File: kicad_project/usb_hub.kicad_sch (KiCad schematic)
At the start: 52 parts, among them J1 USB4105-GF-A, J2 UJ2-ADH-3-TH, U2 CY7C65632-48AXCT, U3 USBLC6-2SC6, U4 USBLC6-2SC6, U5 USBLC6-2SC6, U6 BD2221G-LBTR, U7 BD2221G-LBTR

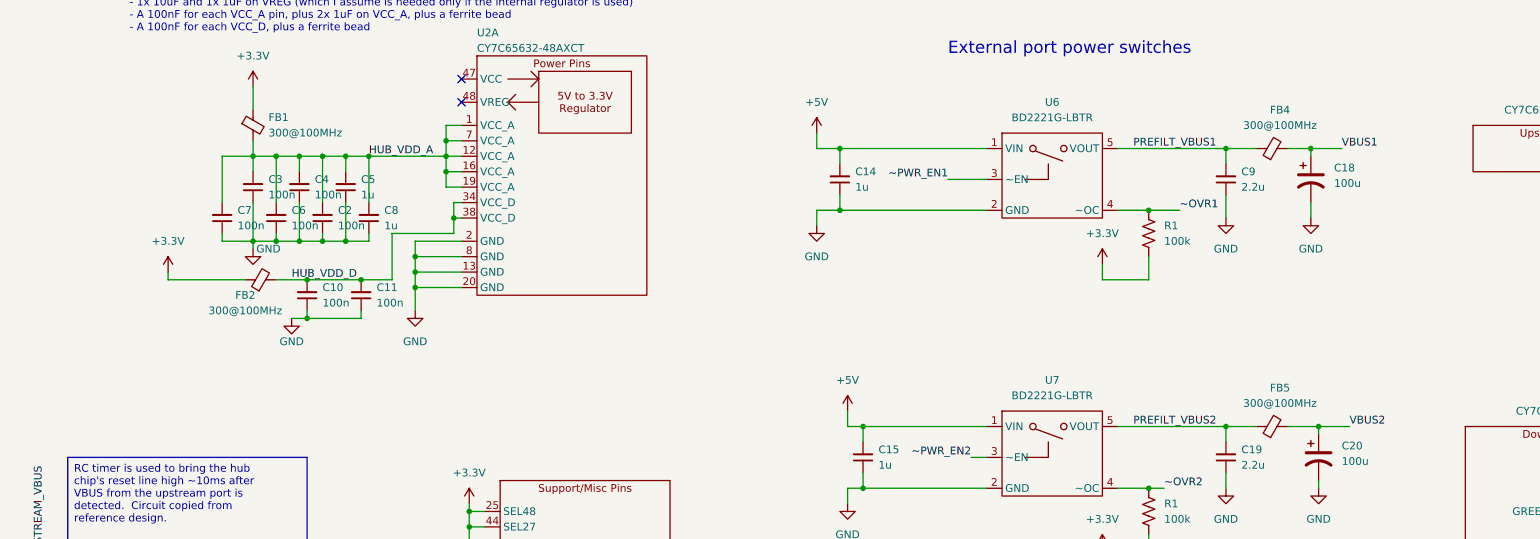
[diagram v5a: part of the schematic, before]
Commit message: Add logo to PCB, add last labels, fix DRC
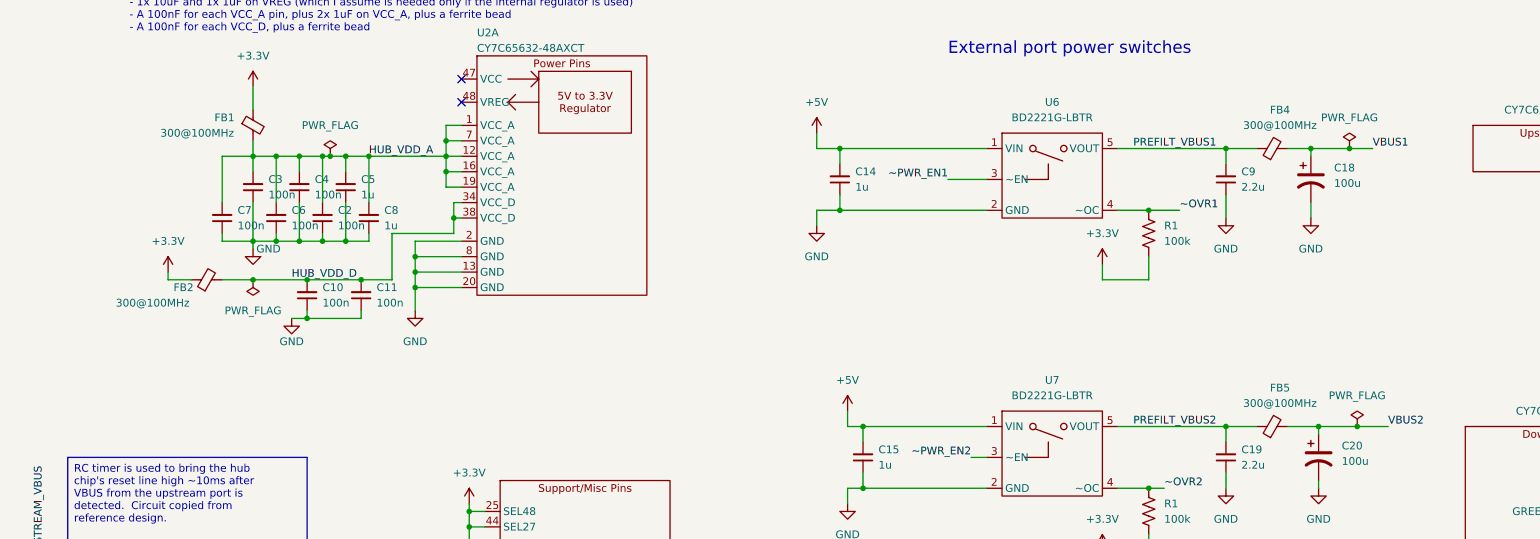
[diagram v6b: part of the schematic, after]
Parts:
- J1: footprint Connector_USB:USB_C_Receptacle_GCT_USB4105-xx-A_16P_TopMnt_Horizontal -> project libraries:USB_C_Receptacle_GCT_USB4105-xx-A_16P_TopMnt_Horizontal-ExtraHoleClearance
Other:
- moved on the sheet: FB2
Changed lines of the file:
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@@
   (junction (at 62.23 48.26) (diameter 0) (color 0 0 0 0)
   )
+  (junction (at 240.03 92.71) (diameter 0) (color 0 0 0 0)
+  )
   (junction (at 68.58 240.03) (diameter 0) (color 0 0 0 0)
   )
@@
   (junction (at 66.04 48.26) (diameter 0) (color 0 0 0 0)
   )
+  (junction (at 238.76 46.99) (diameter 0) (color 0 0 0 0)
+  )
   (junction (at 62.23 62.23) (diameter 0) (color 0 0 0 0)
   )
@@
   (junction (at 335.28 229.87) (diameter 0) (color 0 0 0 0)
   )
+  (junction (at 71.12 48.26) (diameter 0) (color 0 0 0 0)
+  )
   (junction (at 85.09 67.31) (diameter 0) (color 0 0 0 0)
   )
@@
   (junction (at 93.98 109.22) (diameter 0) (color 0 0 0 0)
   )
+  (junction (at 58.42 68.58) (diameter 0) (color 0 0 0 0)
+  )
   (junction (at 347.98 120.65) (diameter 0) (color 0 0 0 0)
   )
@@
     (stroke (width 0) (type default))
   )
-  (wire (pts (xy 62.23 68.58) (xy 67.31 68.58))
+  (wire (pts (xy 53.34 68.58) (xy 58.42 68.58))
     (stroke (width 0) (type default))
   )
@@
     (stroke (width 0) (type default))
   )
-  (wire (pts (xy 44.45 68.58) (xy 57.15 68.58))
+  (wire (pts (xy 44.45 68.58) (xy 48.26 68.58))
     (stroke (width 0) (type default))
   )
@@
     (stroke (width 0) (type default))
   )
-  (wire (pts (xy 233.68 92.71) (xy 238.76 92.71))
+  (wire (pts (xy 233.68 92.71) (xy 240.03 92.71))
     (stroke (width 0) (type default))
   )
@@
     (stroke (width 0) (type default))
   )
-  (wire (pts (xy 232.41 46.99) (xy 237.49 46.99))
-    (stroke (width 0) (type default))
-  )
   (wire (pts (xy 318.77 214.63) (xy 318.77 219.71))
     (stroke (width 0) (type default))
@@
     (stroke (width 0) (type default))
   )
+  (wire (pts (xy 238.76 46.99) (xy 242.57 46.99))
+    (stroke (width 0) (type default))
+  )
   (wire (pts (xy 182.88 205.74) (xy 199.39 205.74))
     (stroke (width 0) (type default))
@@
     (stroke (width 0) (type default))
   )
+  (wire (pts (xy 71.12 48.26) (xy 69.85 48.26))
+    (stroke (width 0) (type default))
+  )
   (wire (pts (xy 335.28 229.87) (xy 351.79 229.87))
     (stroke (width 0) (type default))
@@
     (stroke (width 0) (type default))
   )
-  (wire (pts (xy 73.66 48.26) (xy 69.85 48.26))
+  (wire (pts (xy 73.66 48.26) (xy 71.12 48.26))
     (stroke (width 0) (type default))
   )
@@
     (stroke (width 0) (type default))
   )
+  (wire (pts (xy 232.41 46.99) (xy 238.76 46.99))
+    (stroke (width 0) (type default))
+  )
   (wire (pts (xy 344.17 133.35) (xy 360.68 133.35))
     (stroke (width 0) (type default))
@@
     (stroke (width 0) (type default))
   )
+  (wire (pts (xy 58.42 68.58) (xy 67.31 68.58))
+    (stroke (width 0) (type default))
+  )
   (wire (pts (xy 241.3 213.36) (xy 241.3 215.9))
     (stroke (width 0) (type default))
@@
     (stroke (width 0) (type default))
   )
+  (wire (pts (xy 240.03 92.71) (xy 245.11 92.71))
+    (stroke (width 0) (type default))
+  )
   (wire (pts (xy 204.47 218.44) (xy 204.47 228.6))
     (stroke (width 0) (type default))
@@
     (effects (font (size 1.27 1.27)) (justify left bottom))
   )
-  (label "VBUS2" (at 238.76 92.71 0) (fields_autoplaced)
+  (label "VBUS2" (at 245.11 92.71 0) (fields_autoplaced)
     (effects (font (size 1.27 1.27)) (justify left bottom))
   )
@@
     (effects (font (size 1.27 1.27)) (justify left bottom))
   )
-  (label "VBUS1" (at 237.49 46.99 0) (fields_autoplaced)
+  (label "VBUS1" (at 242.57 46.99 0) (fields_autoplaced)
     (effects (font (size 1.27 1.27)) (justify left bottom))
   )
@@
     )
   )
+  (symbol (lib_id "power:PWR_FLAG") (at 58.42 68.58 180) (unit 1)
+    (in_bom yes) (on_board yes) (dnp no) (fields_autoplaced)
+    (property "Reference" "#FLG05" (at 58.42 70.485 0)
+      (effects (font (size 1.27 1.27)) hide)
+    )
+    (property "Value" "PWR_FLAG" (at 58.42 73.66 0)
+      (effects (font (size 1.27 1.27)))
+    )
+    (property "Footprint" "" (at 58.42 68.58 0)
+      (effects (font (size 1.27 1.27)) hide)
+    )
+    (property "Datasheet" "~" (at 58.42 68.58 0)
+      (effects (font (size 1.27 1.27)) hide)
+    )
+    (pin "1")
+    (instances
+      (project "mbed-ce-ci-shield-v2"
+        (path "/a0f40274-9469-4bcf-885c-e8b8a490ea54/d2cb7c4f-a03f-4f1c-8cab-0427a0ad2909"
+          (reference "#FLG05") (unit 1)
+        )
+      )
+    )
+  )
   (symbol (lib_id "power:+5V") (at 156.21 90.17 0) (unit 1)
     (in_bom yes) (on_board yes) (dnp no) (fields_autoplaced)
@@
     )
   )
+  (symbol (lib_id "power:PWR_FLAG") (at 238.76 46.99 0) (unit 1)
+    (in_bom yes) (on_board yes) (dnp no) (fields_autoplaced)
+    (property "Reference" "#FLG06" (at 238.76 45.085 0)
+      (effects (font (size 1.27 1.27)) hide)
+    )
+    (property "Value" "PWR_FLAG" (at 238.76 41.91 0)
+      (effects (font (size 1.27 1.27)))
+    )
+    (property "Footprint" "" (at 238.76 46.99 0)
+      (effects (font (size 1.27 1.27)) hide)
+    )
+    (property "Datasheet" "~" (at 238.76 46.99 0)
+      (effects (font (size 1.27 1.27)) hide)
+    )
+    (pin "1")
+    (instances
+      (project "mbed-ce-ci-shield-v2"
+        (path "/a0f40274-9469-4bcf-885c-e8b8a490ea54/d2cb7c4f-a03f-4f1c-8cab-0427a0ad2909"
+          (reference "#FLG06") (unit 1)
+        )
+      )
+    )
+  )
   (symbol (lib_id "Device:C_Polarized_US") (at 232.41 52.07 0) (unit 1)
     (in_bom yes) (on_board yes) (dnp no) (fields_autoplaced)
@@
       (effects (font (size 1.27 1.27)) (justify right))
     )
-    (property "Footprint" "Connector_USB:USB_C_Receptacle_GCT_USB4105-xx-A_16P_TopMnt_Horizontal" (at 372.11 57.15 0)
+    (property "Footprint" "project libraries:USB_C_Receptacle_GCT_USB4105-xx-A_16P_TopMnt_Horizontal-ExtraHoleClearance" (at 372.11 57.15 0)
       (effects (font (size 1.27 1.27)) hide)
     )
@@
   )
   (symbol (lib_id "Device:FerriteBead_Small") (at 58.42 43.18 0) (unit 1)
-    (in_bom yes) (on_board yes) (dnp no) (fields_autoplaced)
-    (property "Reference" "FB1" (at 60.96 41.8719 0)
+    (in_bom yes) (on_board yes) (dnp no)
+    (property "Reference" "FB1" (at 52.07 41.91 0)
       (effects (font (size 1.27 1.27)) (justify left))
     )
-    (property "Value" "300@100MHz" (at 60.96 44.4119 0)
+    (property "Value" "300@100MHz" (at 43.18 44.45 0)
       (effects (font (size 1.27 1.27)) (justify left))
     )
@@
     )
   )
+  (symbol (lib_id "power:PWR_FLAG") (at 240.03 92.71 0) (unit 1)
+    (in_bom yes) (on_board yes) (dnp no) (fields_autoplaced)
+    (property "Reference" "#FLG07" (at 240.03 90.805 0)
+      (effects (font (size 1.27 1.27)) hide)
+    )
+    (property "Value" "PWR_FLAG" (at 240.03 87.63 0)
+      (effects (font (size 1.27 1.27)))
+    )
+    (property "Footprint" "" (at 240.03 92.71 0)
+      (effects (font (size 1.27 1.27)) hide)
+    )
+    (property "Datasheet" "~" (at 240.03 92.71 0)
+      (effects (font (size 1.27 1.27)) hide)
+    )
+    (pin "1")
+    (instances
+      (project "mbed-ce-ci-shield-v2"
+        (path "/a0f40274-9469-4bcf-885c-e8b8a490ea54/d2cb7c4f-a03f-4f1c-8cab-0427a0ad2909"
+          (reference "#FLG07") (unit 1)
+        )
+      )
+    )
+  )
   (symbol (lib_id "power:GND") (at 68.58 243.84 0) (unit 1)
     (in_bom yes) (on_board yes) (dnp no)
@@
     )
   )
+  (symbol (lib_id "power:PWR_FLAG") (at 71.12 48.26 0) (unit 1)
+    (in_bom yes) (on_board yes) (dnp no) (fields_autoplaced)
+    (property "Reference" "#FLG04" (at 71.12 46.355 0)
+      (effects (font (size 1.27 1.27)) hide)
+    )
+    (property "Value" "PWR_FLAG" (at 71.12 43.18 0)
+      (effects (font (size 1.27 1.27)))
+    )
+    (property "Footprint" "" (at 71.12 48.26 0)
+      (effects (font (size 1.27 1.27)) hide)
+    )
+    (property "Datasheet" "~" (at 71.12 48.26 0)
+      (effects (font (size 1.27 1.27)) hide)
+    )
+    (pin "1")
+    (instances
+      (project "mbed-ce-ci-shield-v2"
+        (path "/a0f40274-9469-4bcf-885c-e8b8a490ea54/d2cb7c4f-a03f-4f1c-8cab-0427a0ad2909"
+          (reference "#FLG04") (unit 1)
+        )
+      )
+    )
+  )
   (symbol (lib_id "Device:C_Small") (at 154.94 52.07 180) (unit 1)
     (in_bom yes) (on_board yes) (dnp no) (fields_autoplaced)
@@
     )
   )
-  (symbol (lib_id "Device:FerriteBead_Small") (at 59.69 68.58 90) (unit 1)
+  (symbol (lib_id "Device:FerriteBead_Small") (at 50.8 68.58 90) (unit 1)
     (in_bom yes) (on_board yes) (dnp no)
-    (property "Reference" "FB2" (at 57.15 71.12 90)
+    (property "Reference" "FB2" (at 46.99 69.85 90)
       (effects (font (size 1.27 1.27)))
     )
-    (property "Value" "300@100MHz" (at 57.15 73.66 90)
+    (property "Value" "300@100MHz" (at 41.91 72.39 90)
       (effects (font (size 1.27 1.27)))
     )
-    (property "Footprint" "Resistor_SMD:R_1206_3216Metric" (at 59.69 70.358 90)
+    (property "Footprint" "Resistor_SMD:R_1206_3216Metric" (at 50.8 70.358 90)
       (effects (font (size 1.27 1.27)) hide)
     )
-    (property "Datasheet" "~" (at 59.69 68.58 0)
+    (property "Datasheet" "~" (at 50.8 68.58 0)
       (effects (font (size 1.27 1.27)) hide)
     )
-    (property "SKU" "732-4654-1-ND" (at 59.69 68.58 0)
+    (property "SKU" "732-4654-1-ND" (at 50.8 68.58 0)
       (effects (font (size 1.27 1.27)) hide)
     )

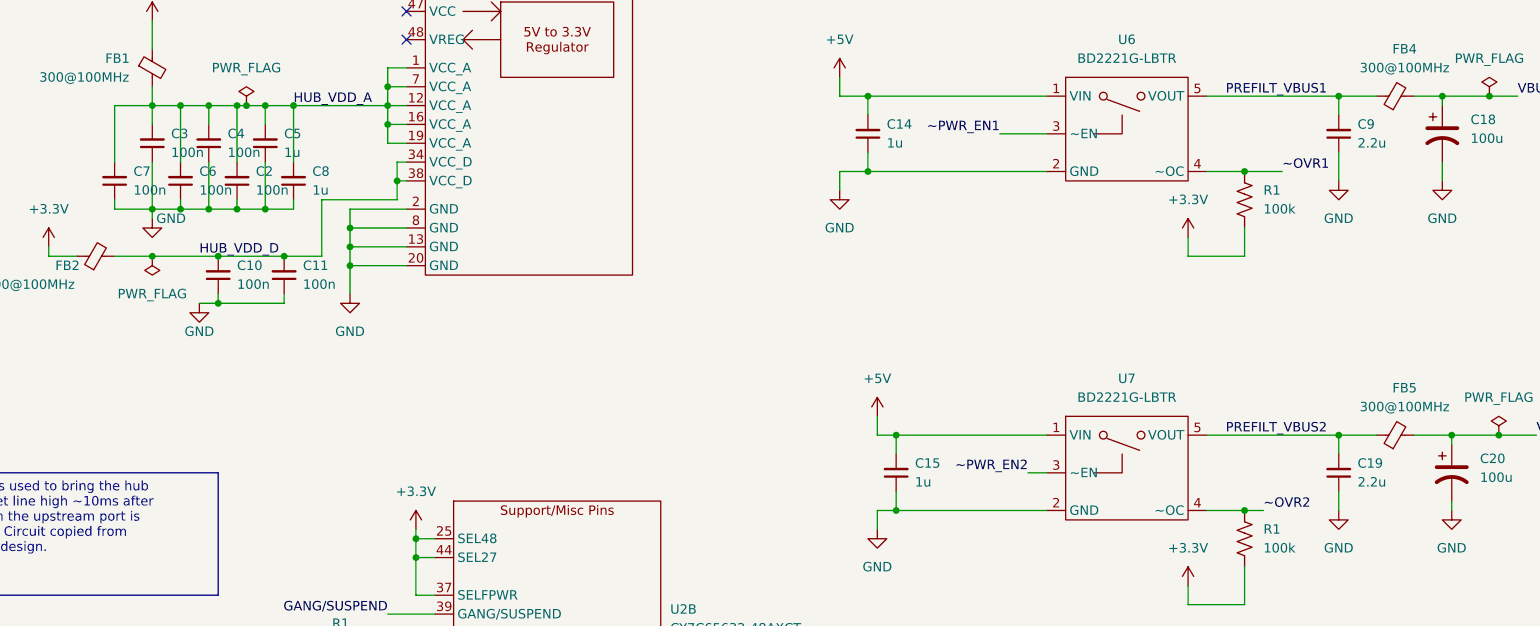
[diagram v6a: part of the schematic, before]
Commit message: Add part numbers for capacitors, start working on BoM job
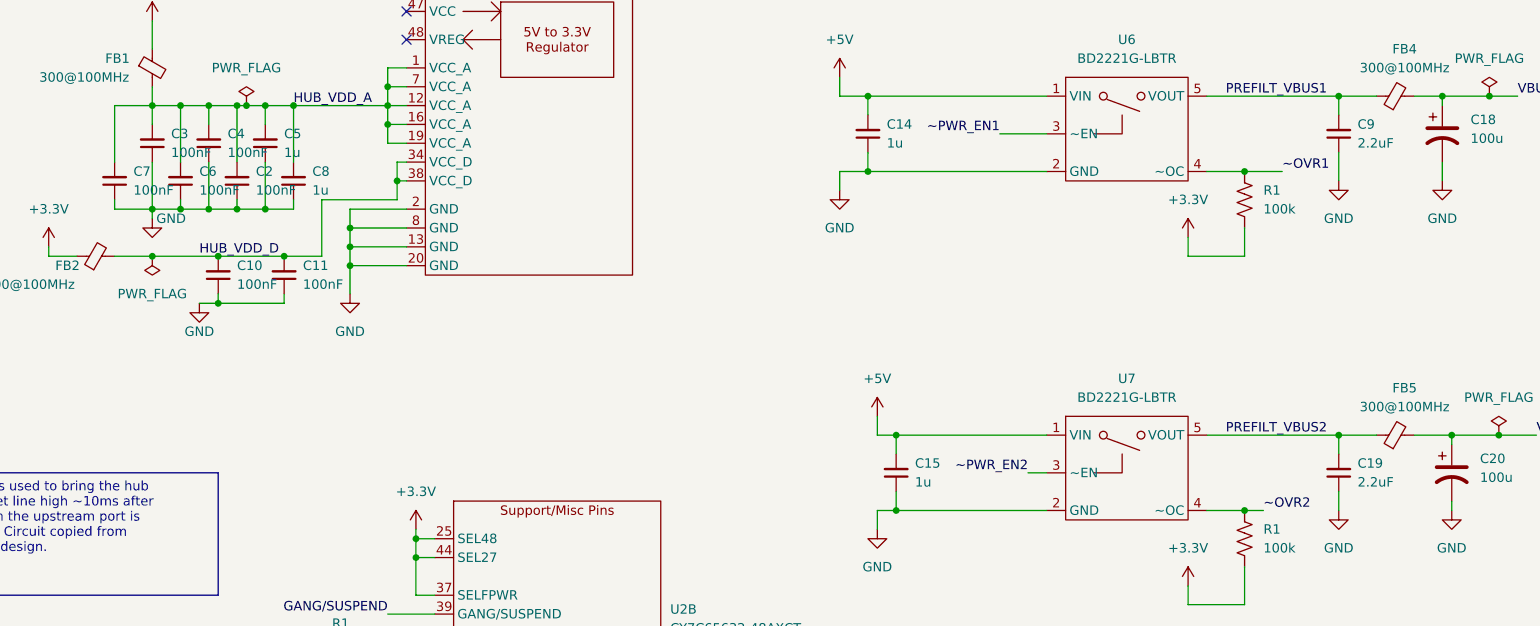
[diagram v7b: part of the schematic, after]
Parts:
- C10, C11, C2, C3, C4, C6, C7: value 100n -> 100nF; LibRef (none) -> GRM319R72A104KA01D; Supplier (none) -> Digi-Key
- C14, C15, C21, C5, C8: LibRef (none) -> CL31B105KBHNNNE; Supplier (none) -> Digi-Key
- C18: LibRef (none) -> RL81V101MDN1KX; Supplier (none) -> Digi-Key
- C19, C9: value 2.2u -> 2.2uF; LibRef (none) -> CL31B225KBHNNNE; SKU (none) -> 1276-1291-1-ND; Supplier (none) -> Digi-Key
- C20: LibRef (none) -> RL81V101MDN1KX; SKU (none) -> 493-6630-1-ND; Supplier (none) -> Digi-Key
- D1, D2, D3, D4, D5, FB1, FB2, FB4, FB5, J1, J2, R1, U2, U3, U4, U5, U6, U7: Supplier (none) -> Digi-Key
